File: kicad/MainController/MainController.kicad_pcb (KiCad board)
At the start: 2 copper layers, 120 x 75 mm, 45 parts, among them J1 Controller, J10 Barrel_Jack_Switch, J11 Pwr, J2 Screen, J3 JTAG, J4 H-Bridge, J5 Lamp, J7 RGB, J8 Winch, J9 Motor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

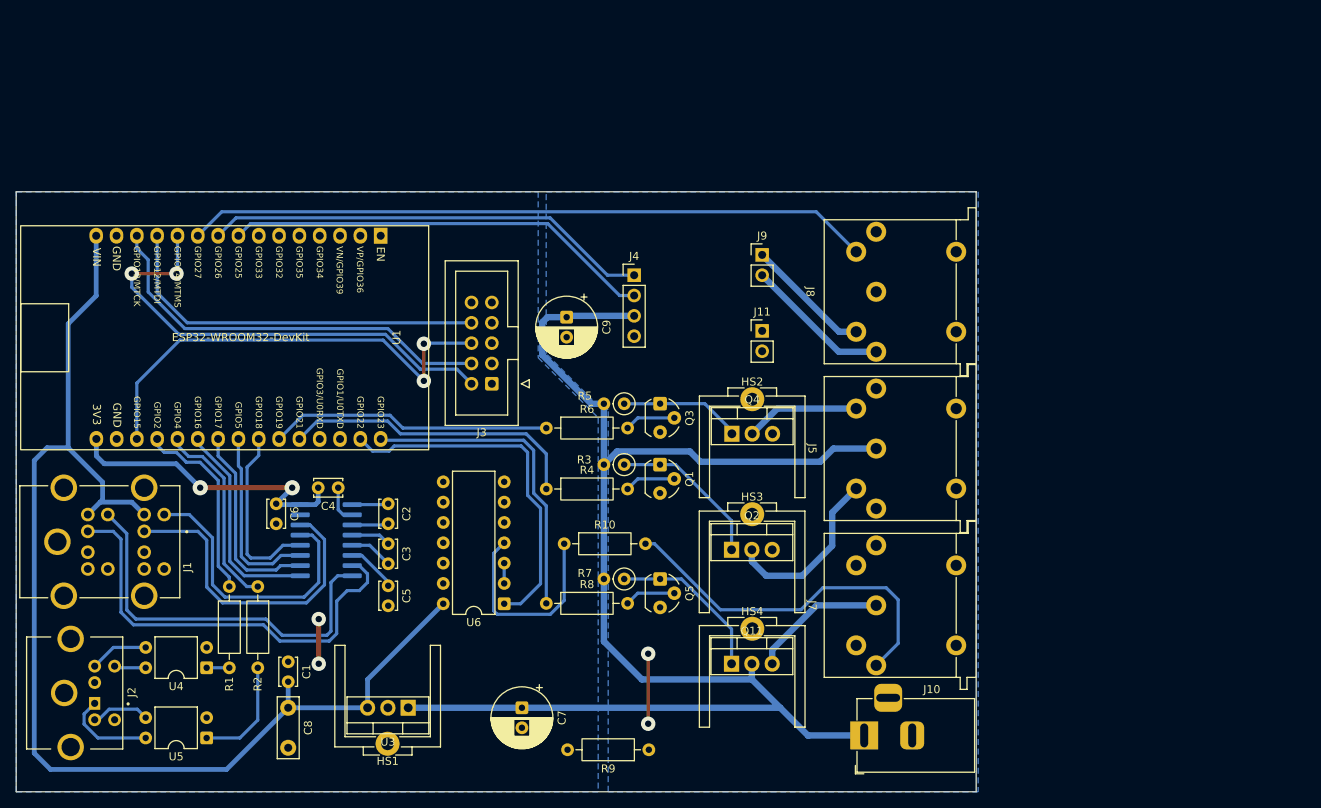
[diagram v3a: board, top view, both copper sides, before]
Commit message: Fixed footprints for MainController board
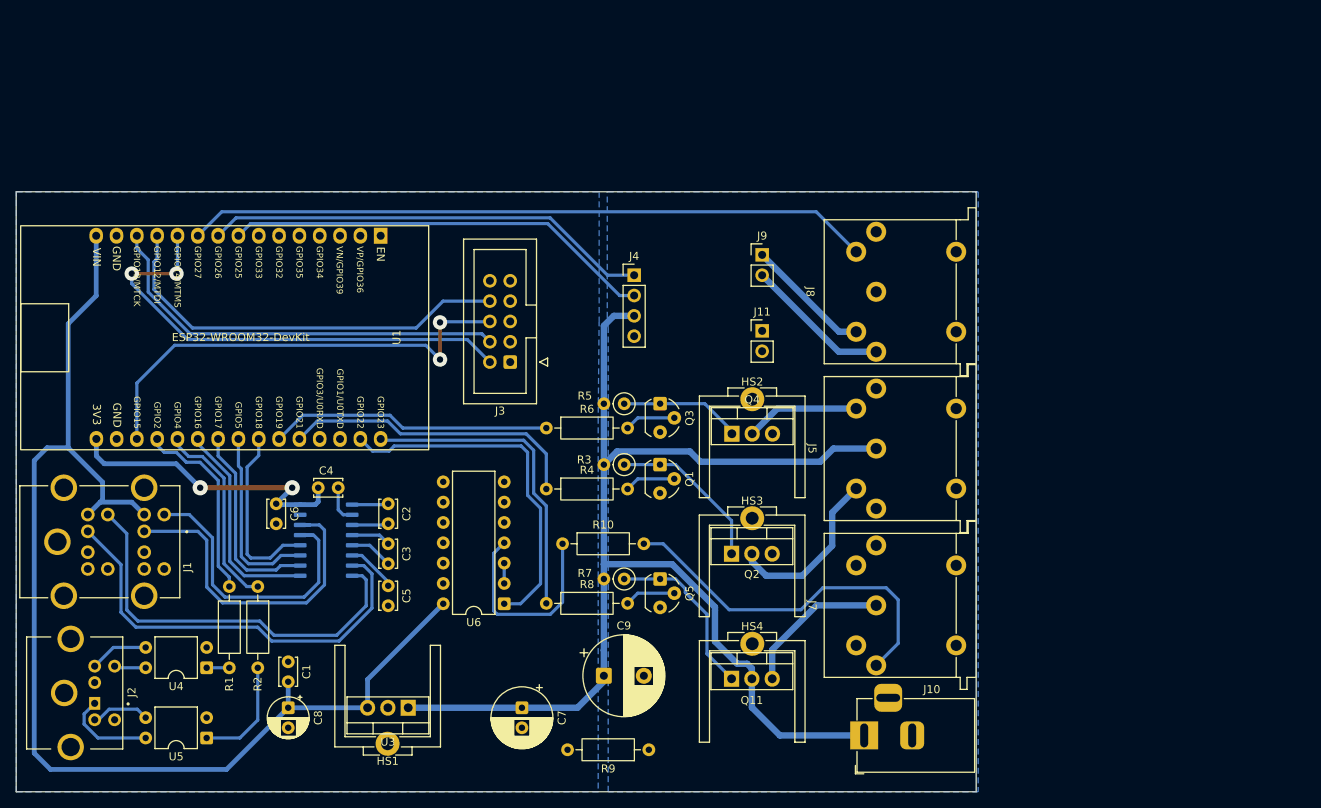
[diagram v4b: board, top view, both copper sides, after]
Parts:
- C1, C2, C3, C4, C5, C6: value 10n -> 100n
- C8: footprint Capacitor_THT:C_Disc_D7.5mm_W2.5mm_P5.00mm -> Capacitor_THT:CP_Radial_D5.0mm_P2.50mm
- C9: value 100u -> 470u; footprint Capacitor_THT:CP_Radial_D7.5mm_P2.50mm -> Capacitor_THT:CP_Radial_D10.0mm_P5.00mm
- R9: value 100 -> 10
- U2: footprint Package_SO:SOIC-16W_5.3x10.2mm_P1.27mm -> Package_SO:SOIC-16_4.55x10.3mm_P1.27mm
- moved C9 45.1 mm to (151.0, 128.5), turned to 0 degrees
- moved J3 3.55 mm to (139.2, 89.3)
- moved HS4 1.88 mm to (169.5, 125.4)
- moved Q11 1.88 mm to (166.9, 128.9)
- moved HS3 0.50 mm to (169.5, 109.7)
- moved Q2 0.50 mm to (166.9, 113.2)
- moved R10 0.20 mm to (145.8, 112.0)
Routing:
- net +12V: track 177.4 -> 157.3 mm
- net GND2: track 8.75 -> 0.00 mm, vias 2 -> 0
- net GND: track 5.59 -> 0.00 mm, vias 2 -> 0
- net /TDI: track 48.0 -> 52.3 mm
- net /PowerConnectors/LED_PWR: track 17.0 -> 18.9 mm
- net /PR_RS232_IN: track 49.1 -> 50.9 mm
- net Net-(Q11-G): track 20.4 -> 21.7 mm
- net /TCK: track 51.7 -> 52.9 mm
- net /KP_RS232_OUT: track 40.1 -> 41.2 mm
- net /TMS: track 59.5 -> 60.4 mm
- net /KP_RS232_IN: track 35.5 -> 36.3 mm

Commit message: Added commandline interface to main controller
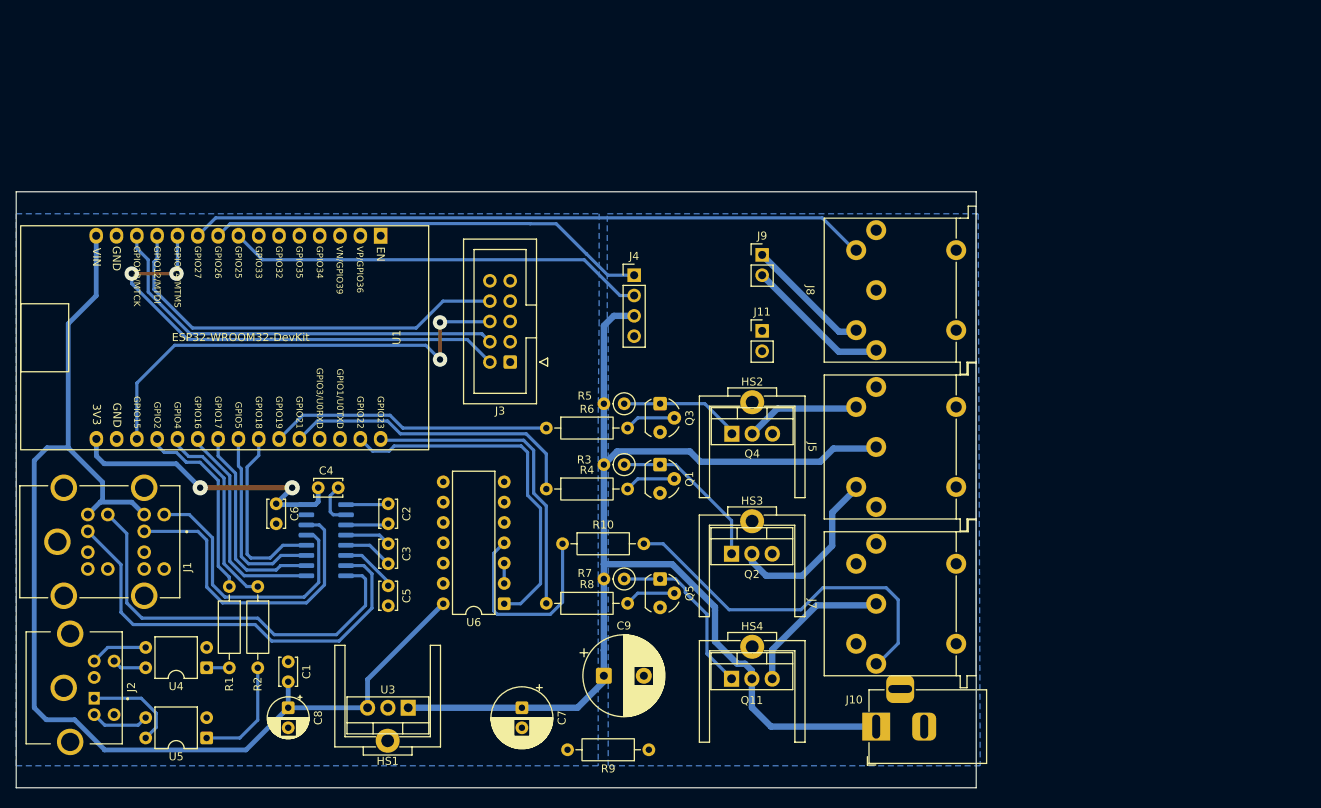
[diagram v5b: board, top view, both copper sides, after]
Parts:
- U2: footprint Package_SO:SOIC-16_4.55x10.3mm_P1.27mm -> Package_SO:SOIC-16_3.9x9.9mm_P1.27mm
- moved J10 1.86 mm to (185.0, 134.9)
- moved J2 0.64 mm to (83.4, 130.0)
- moved J7 0.20 mm to (185.0, 119.5)
- moved J8 0.20 mm to (185.0, 80.3)
- moved J5 0.20 mm to (185.0, 99.9)
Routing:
- net +5V: track 152.3 -> 147.0 mm
- net Net-(U2-VS+): track 4.76 -> 6.67 mm
- net /In1: track 53.8 -> 52.6 mm
- net /PR_RS232_IN: track 50.9 -> 50.2 mm
- net /Switch: track 85.6 -> 85.0 mm
- net Net-(J2-Pad1): track 11.6 -> 12.2 mm
- net Net-(J2-Pad6): track 3.69 -> 4.29 mm
- net /In2: track 55.9 -> 55.3 mm
- net Net-(J2-Pad3): track 6.87 -> 7.37 mm
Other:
- board size 120 x 75 mm -> 120 x 74.5 mm

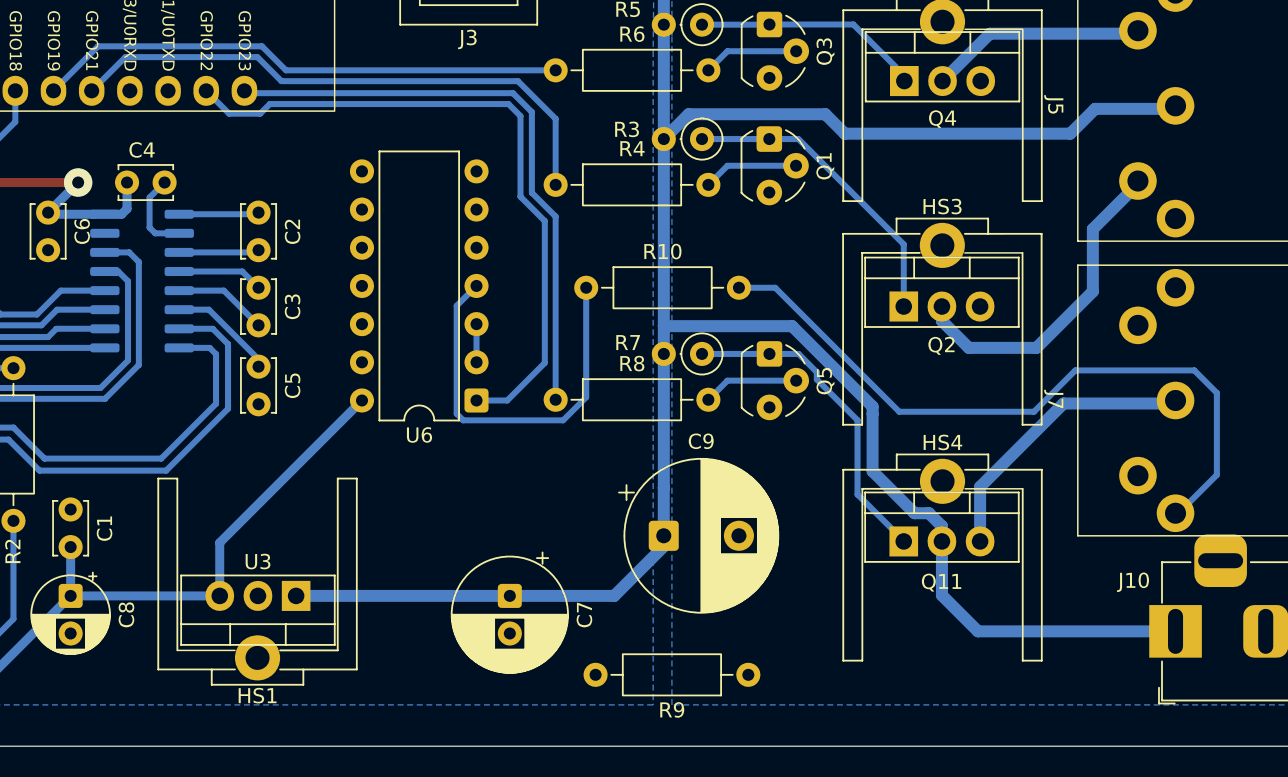
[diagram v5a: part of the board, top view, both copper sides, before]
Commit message: Fixed MainController LED power and data drivers
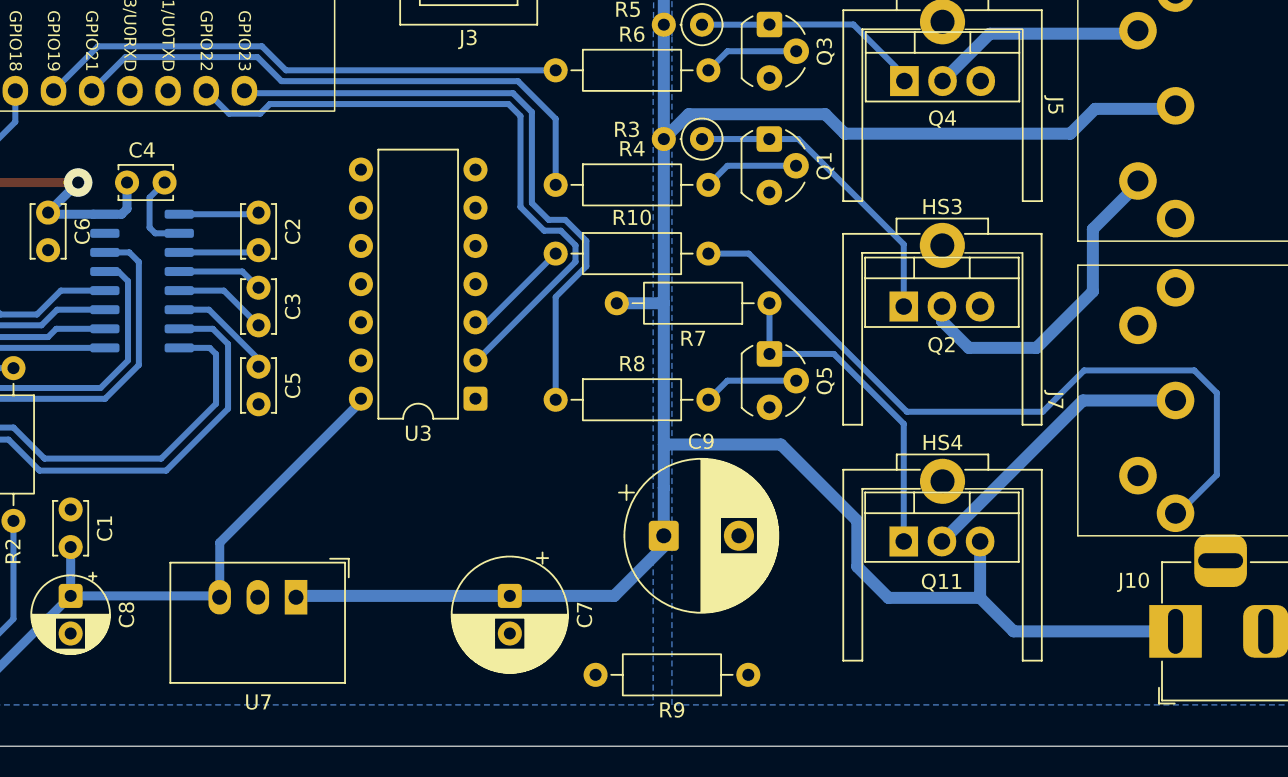
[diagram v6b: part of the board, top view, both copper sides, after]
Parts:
- removed HS1: Heatsink_Pad, Custom_Heatsinks:Heatsink_Aavid_TO-220_H12.7mm
- removed U6: 4069, Package_DIP:DIP-14_W7.62mm
- added U7: LME78_05-1.0, Custom_Converter:Converter_DCDC_GAPTEC_LME78_05-1.0, F.Cu at (126.5, 132.6)
- C8: value 0.1u -> 33u
- R7: footprint Resistor_THT:R_Axial_DIN0207_L6.3mm_D2.5mm_P2.54mm_Vertical -> Resistor_THT:R_Axial_DIN0207_L6.3mm_D2.5mm_P10.16mm_Horizontal
- R9: value 10 -> 0
- U3: value L7805 -> 74LS125; footprint Package_TO_SOT_THT:TO-220-3_Vertical -> Package_DIP:DIP-14_W7.62mm
- moved U3 17.7 mm to (138.4, 119.4)
- moved R7 5.61 mm to (158.0, 113.0)
- moved R10 3.05 mm to (143.8, 109.7)
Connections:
- Q11 pad 2: +12V -> /PowerConnectors/LED_PWR
- Q11 pad 3: /PowerConnectors/LED_PWR -> +12V
- U3 pad 1: +12V -> GND
- U3 pad 2: GND -> /RGB_Data
- U3 pad 3: +5V -> Net-(R10-Pad1)
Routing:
- net Net-(R10-Pad1): track 25.8 -> 7.23 mm
- net Net-(J7-Pad3): track 46.1 -> 49.3 mm
- net Net-(U6-Pad2): track 2.54 -> 0.00 mm
- net /RGB_PWR: track 39.3 -> 41.6 mm
- net /RGB_Data: track 44.8 -> 43.3 mm
- net /KP_RS232_IN: track 36.3 -> 34.9 mm
- net /KP_RS232_OUT: track 41.2 -> 40.0 mm
- net +12V: track 157.2 -> 158.4 mm
- net Net-(U2-VS+): track 6.67 -> 5.55 mm
